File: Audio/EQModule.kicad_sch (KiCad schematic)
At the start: 46 parts, among them J6 AUX_IN, J7 V_IN, J8 AUX_OUT, U2 NJM4558, U3 NJM4558

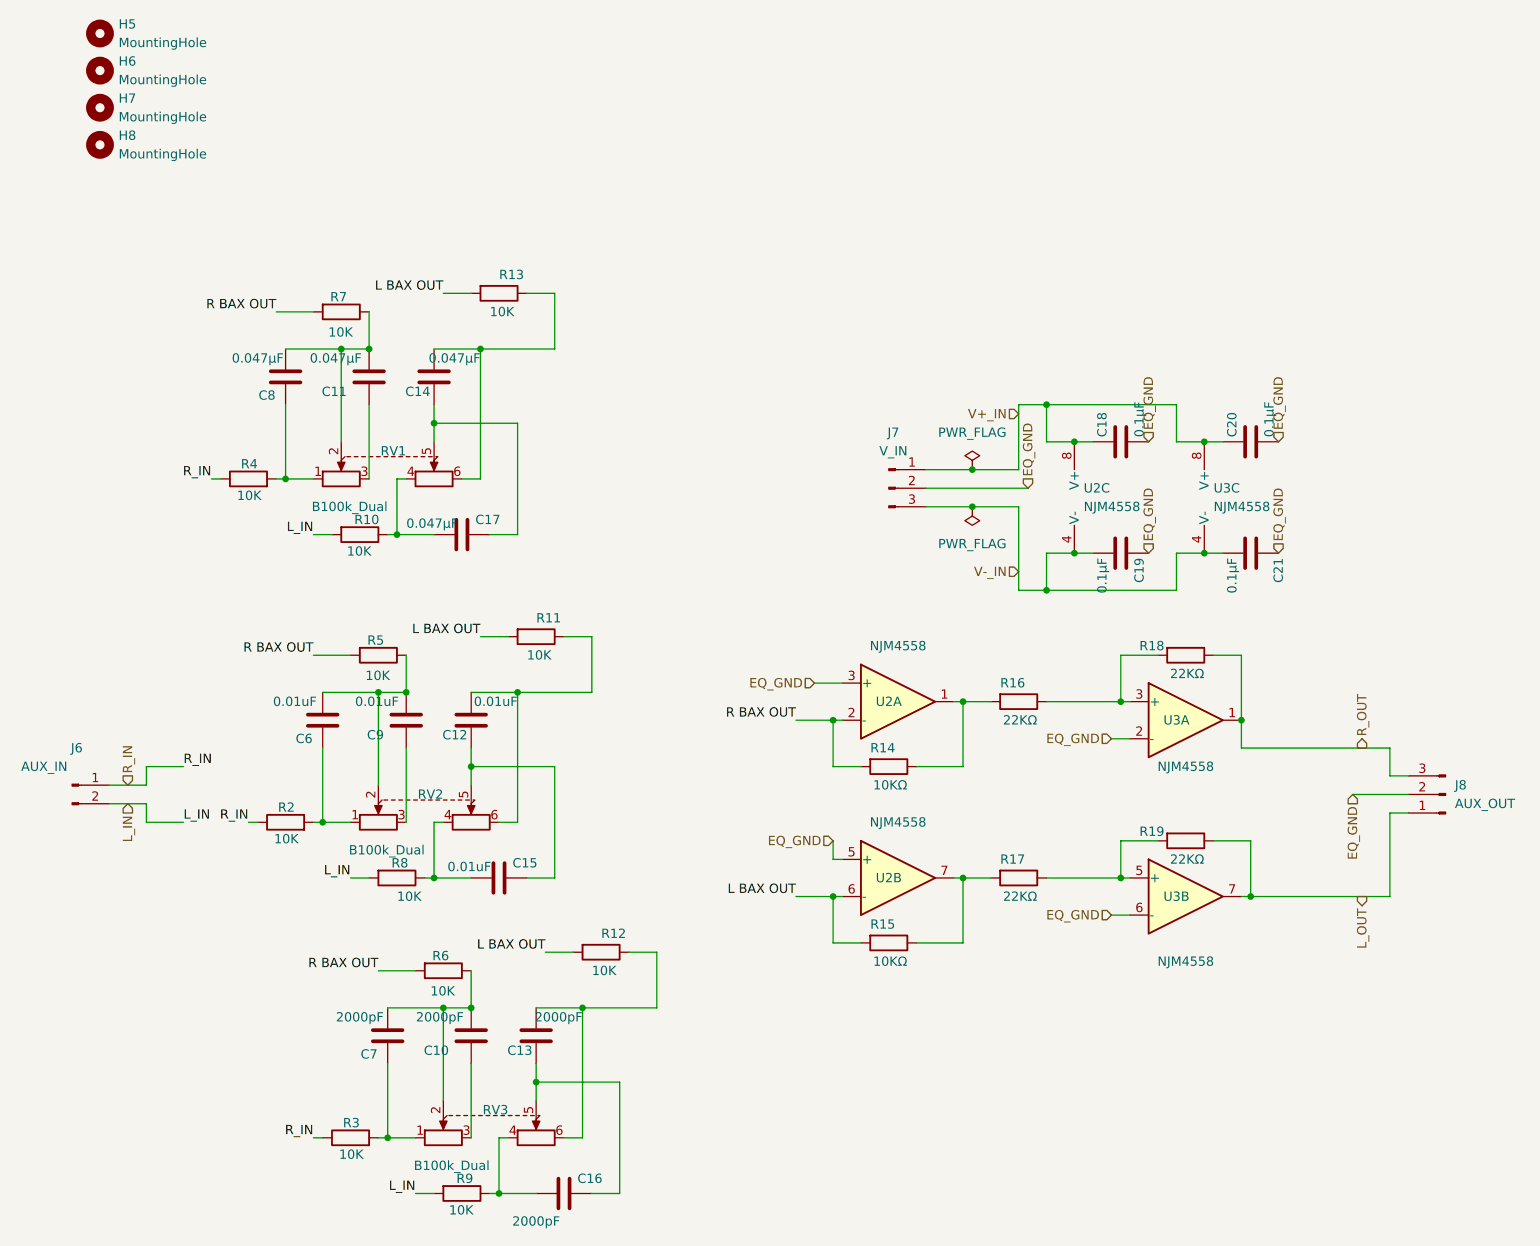
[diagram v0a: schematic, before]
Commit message: add controll module image
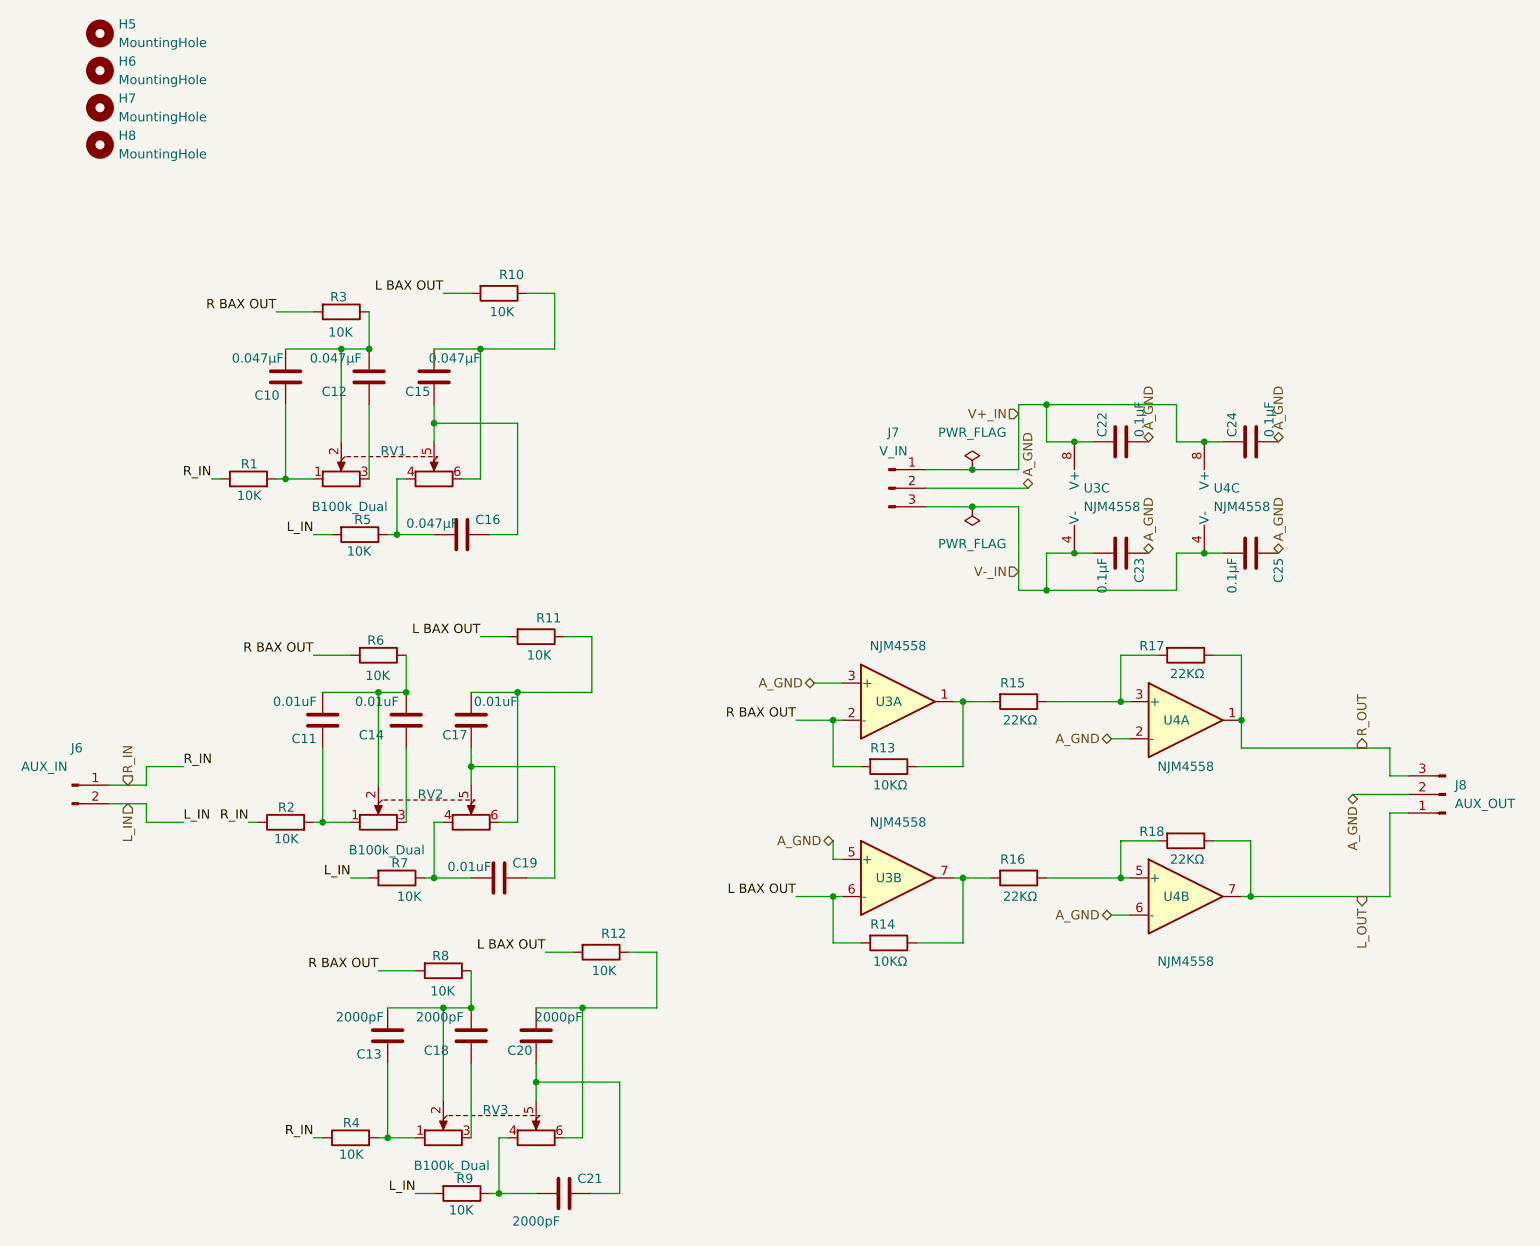
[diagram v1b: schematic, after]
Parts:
- renumbered C8 to C10, C6 to C11, C11 to C12, C7 to C13, C9 to C14, C14 to C15, C17 to C16, C12 to C17, C10 to C18, C15 to C19, C13 to C20, C16 to C21, C18 to C22, C19 to C23, C20 to C24, C21 to C25, R4 to R1, R13 to R10, R14 to R13, R15 to R14, R16 to R15, R17 to R16, R18 to R17, R19 to R18, R7 to R3, R3 to R4, R10 to R5, R5 to R6, R8 to R7, R6 to R8, U2 to U3, U3 to U4
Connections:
- net EQ_GND renamed A_GND

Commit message: rework pcb
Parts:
- C10, C12, C15, C16: footprint Capacitor_THT:C_Rect_L7.2mm_W4.5mm_P5.00mm_FKS2_FKP2_MKS2_MKP2 -> Capacitor_THT:C_Rect_L7.2mm_W3.5mm_P5.00mm_FKS2_FKP2_MKS2_MKP2
- C11, C14, C17, C19: footprint Capacitor_THT:C_Rect_L7.2mm_W2.5mm_P5.00mm_FKS2_FKP2_MKS2_MKP2 -> Capacitor_THT:C_Rect_L7.2mm_W3.0mm_P5.00mm_FKS2_FKP2_MKS2_MKP2
- C13, C18, C20, C21: value 2000pF -> 2200pF; footprint Capacitor_THT:C_Rect_L13.0mm_W6.0mm_P10.00mm_FKS3_FKP3_MKS4 -> Capacitor_THT:C_Rect_L7.2mm_W4.5mm_P5.00mm_FKS2_FKP2_MKS2_MKP2
- C22, C23, C24, C25: footprint Resistor_SMD:R_0603_1608Metric_Pad0.98x0.95mm_HandSolder -> Capacitor_SMD:C_1206_3216Metric_Pad1.33x1.80mm_HandSolder
- R1, R10, R11, R12, R13, R14, R15, R16, R17, R18, R2, R3, R4, R5, R6, R7, R8, R9: footprint Resistor_SMD:R_0603_1608Metric_Pad0.98x0.95mm_HandSolder -> Resistor_SMD:R_1206_3216Metric_Pad1.30x1.75mm_HandSolder
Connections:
- net A_GND: now also U4.3 (+), U4.5 (+); no longer U4.2 (-), U4.6 (-)
- net at R16.1, R18.2: now also U4.6 (-); no longer U4.5 (+)
- net at R15.1, R17.2: now also U4.2 (-); no longer U4.3 (+)
